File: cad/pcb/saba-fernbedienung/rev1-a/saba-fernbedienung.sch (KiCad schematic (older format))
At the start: 0 parts

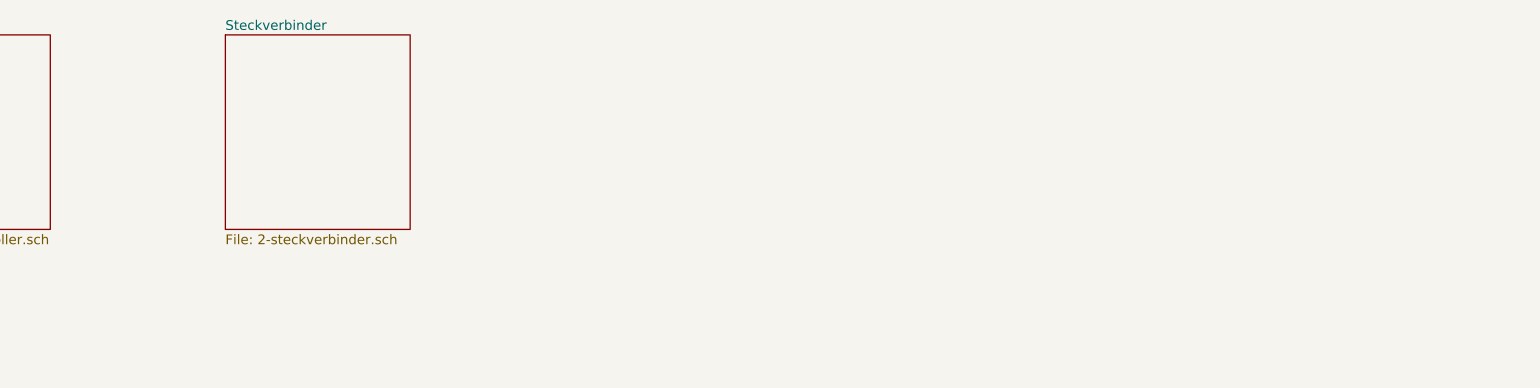
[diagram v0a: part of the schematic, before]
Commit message: Add: Steuerschaltung, Codec, Audio
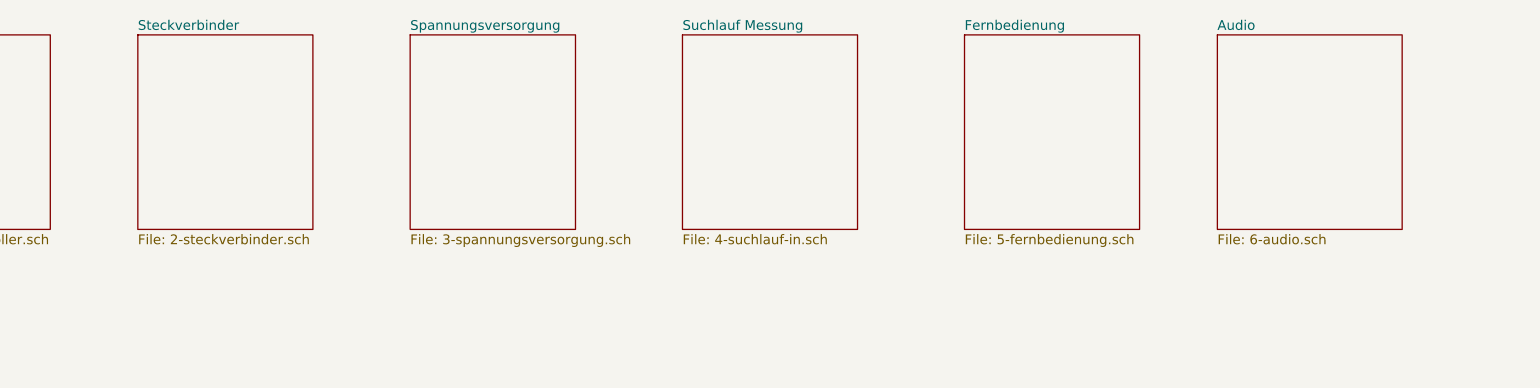
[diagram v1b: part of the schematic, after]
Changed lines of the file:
@@
 $Descr A4 11693 8268
 encoding utf-8
-Sheet 1 3
+Sheet 1 7
 Title "Fernbedienung SABA 6-3D"
-Date "2021-01-11"
+Date "2021-01-13"
 Rev "1-A"
 Comp "Martin Wagner DL2WAG"
 Comment1 "Lizenz: CERN-OHL-W (OHL v2)"
-Comment2 ""
+Comment2 "Microcontroller + Umgebung"
 Comment3 "(Meersburg/Freiburg 6-3D, weitere?)"
 Comment4 "Fernbedienung für SABA \"Automatic\" Radios"
@@
 $EndComp
 $Sheet
-S 2850 950  950  1000
+S 2400 950  900  1000
 U 6002EA57
 F0 "Steckverbinder" 50
 F1 "2-steckverbinder.sch" 50
 $EndSheet
+$Sheet
+S 3800 950  850  1000
+U 6008B538
+F0 "Spannungsversorgung" 50
+F1 "3-spannungsversorgung.sch" 50
+$EndSheet
+$Sheet
+S 5200 950  900  1000
+U 60135668
+F0 "Suchlauf Messung" 50
+F1 "4-suchlauf-in.sch" 50
+$EndSheet
+$Sheet
+S 6650 950  900  1000
+U 6044FE50
+F0 "Fernbedienung" 50
+F1 "5-fernbedienung.sch" 50
+$EndSheet
+$Sheet
+S 7950 950  950  1000
+U 6041BFCD
+F0 "Audio" 50
+F1 "6-audio.sch" 50
+$EndSheet
 $EndSCHEMATC
